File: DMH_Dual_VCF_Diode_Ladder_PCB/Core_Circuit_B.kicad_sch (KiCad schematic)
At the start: 53 parts, among them SW1 SW_SPDT, SW2 SW_SPDT, SW3 SW_SPDT, SW5 Switch_SP3T_APEM5244, U1 TL074, U2 TL074

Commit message: Schematic design in progress
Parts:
- renumbered C11 to C18, C12 to C19, C15 to C20, C13 to C21, C14 to C22, C7 to C3, C10 to C6, D14 to D15, D13 to D16, D7 to D17, D8 to D18, D9 to D19, D10 to D20, D11 to D21, D12 to D22, D6 to D23, R19 to R63, R18 to R64, R14 to R65, R16 to R66, R5 to R67, R17 to R68, R15 to R69, R6 to R70, R21 to R71, R2 to R72, R20 to R73, R23 to R74, R1 to R75, R22 to R76, R3 to R77, R7 to R78, R10 to R79, R13 to R80, R11 to R81, R4 to R82, R9 to R83, R8 to R84, R12 to R85, R61 to R86, R24 to R87, R62 to R88, RV1 to RV16, RV2 to RV17, RV3 to RV18, RV4 to RV19, RV6 to RV5, SW5 to SW10, SW3 to SW7, SW1 to SW8, SW2 to SW9, U1 to U5, U2 to U6

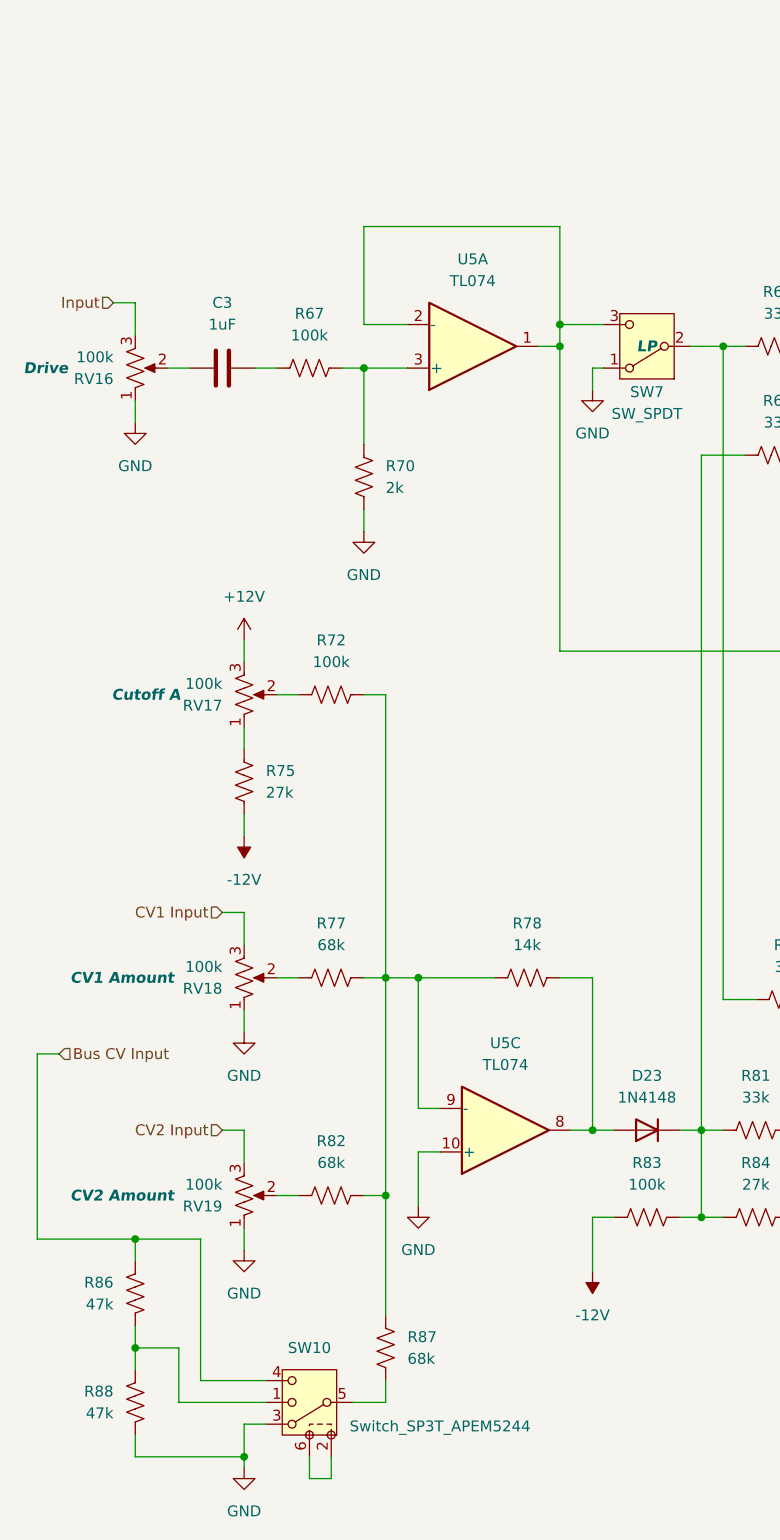
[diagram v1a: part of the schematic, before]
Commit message: Made CV processing page
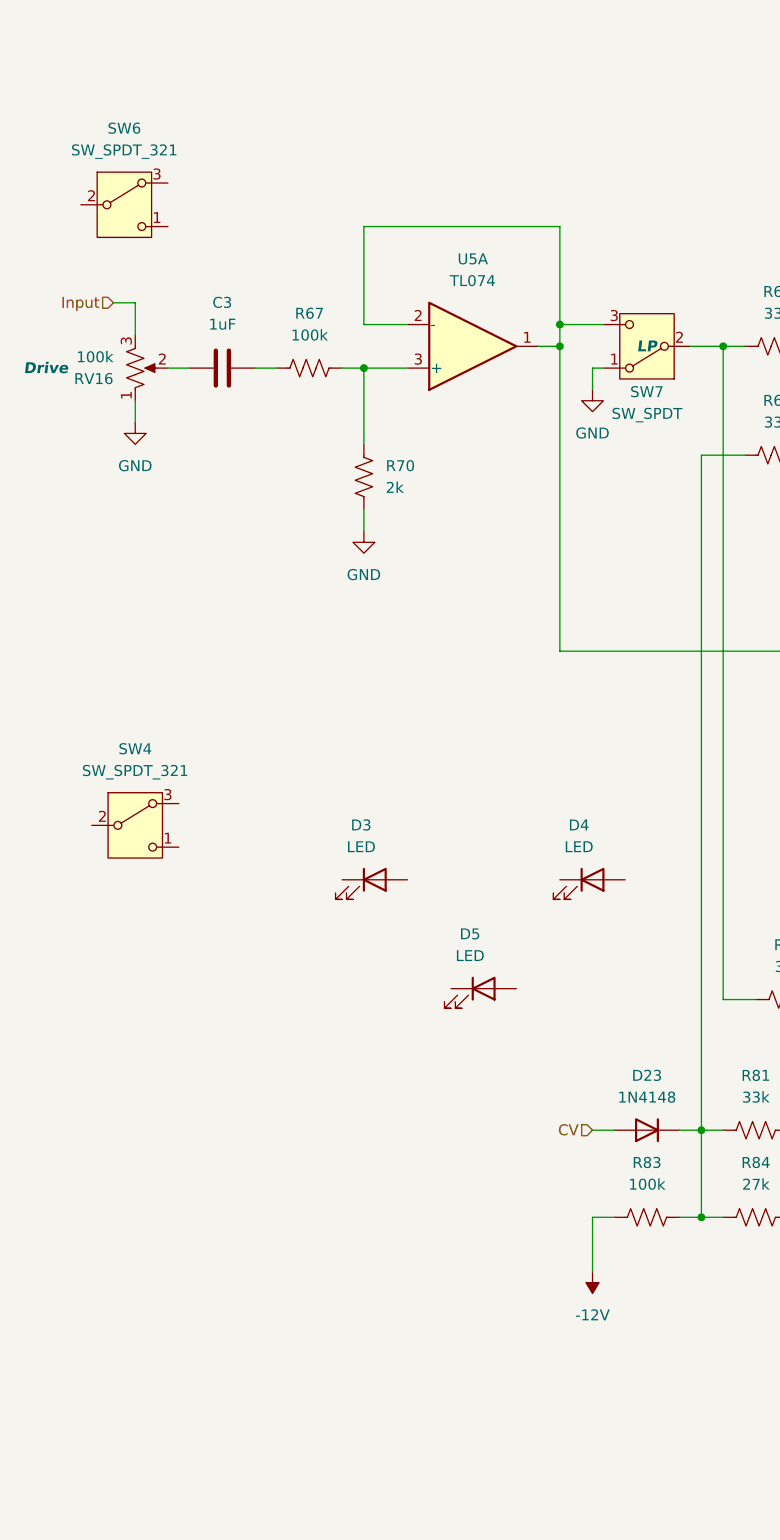
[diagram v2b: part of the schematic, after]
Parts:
- removed R72: 100k, Resistor_THT:R_Axial_DIN0207_L6.3mm_D2.5mm_P7.62mm_Horizontal, symbol Device:R_US
- removed R75: 27k, Resistor_THT:R_Axial_DIN0207_L6.3mm_D2.5mm_P7.62mm_Horizontal, symbol Device:R_US
- removed R77, R82, R87: 68k, Resistor_THT:R_Axial_DIN0207_L6.3mm_D2.5mm_P7.62mm_Horizontal, symbol Device:R_US
- removed R78: 14k, Resistor_THT:R_Axial_DIN0207_L6.3mm_D2.5mm_P7.62mm_Horizontal, symbol Device:R_US
- removed R86, R88: 47k, Resistor_THT:R_Axial_DIN0207_L6.3mm_D2.5mm_P7.62mm_Horizontal, symbol Device:R_US
- removed RV17: 100k, SynthStuff:Potentiometer_Alpha_RD901F-40-00D_Single_Vertical, symbol Device:R_Potentiometer_US
- removed RV18, RV19: 100k, SynthStuff:Potentiometer_TT_P110KH1, symbol Device:R_Potentiometer_US
- removed SW10: Switch_SP3T_APEM5244, symbol SynthStuff:Switch_SP3T
- removed unit 3 of U5
- added D3, D4, D5: LED, LED_THT:LED_D3.0mm, symbol Device:LED
- added SW4, SW6: SW_SPDT_321, SynthStuff:Toggle_Switch_THT, symbol Switch:SW_SPDT_321
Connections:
- net CV: now reaches D23.2 (A)

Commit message: Finished designing circuit
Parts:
- removed D3, D4, D5: LED, LED_THT:LED_D3.0mm, symbol Device:LED
- removed SW4, SW6: SW_SPDT_321, SynthStuff:Toggle_Switch_THT, symbol Switch:SW_SPDT_321

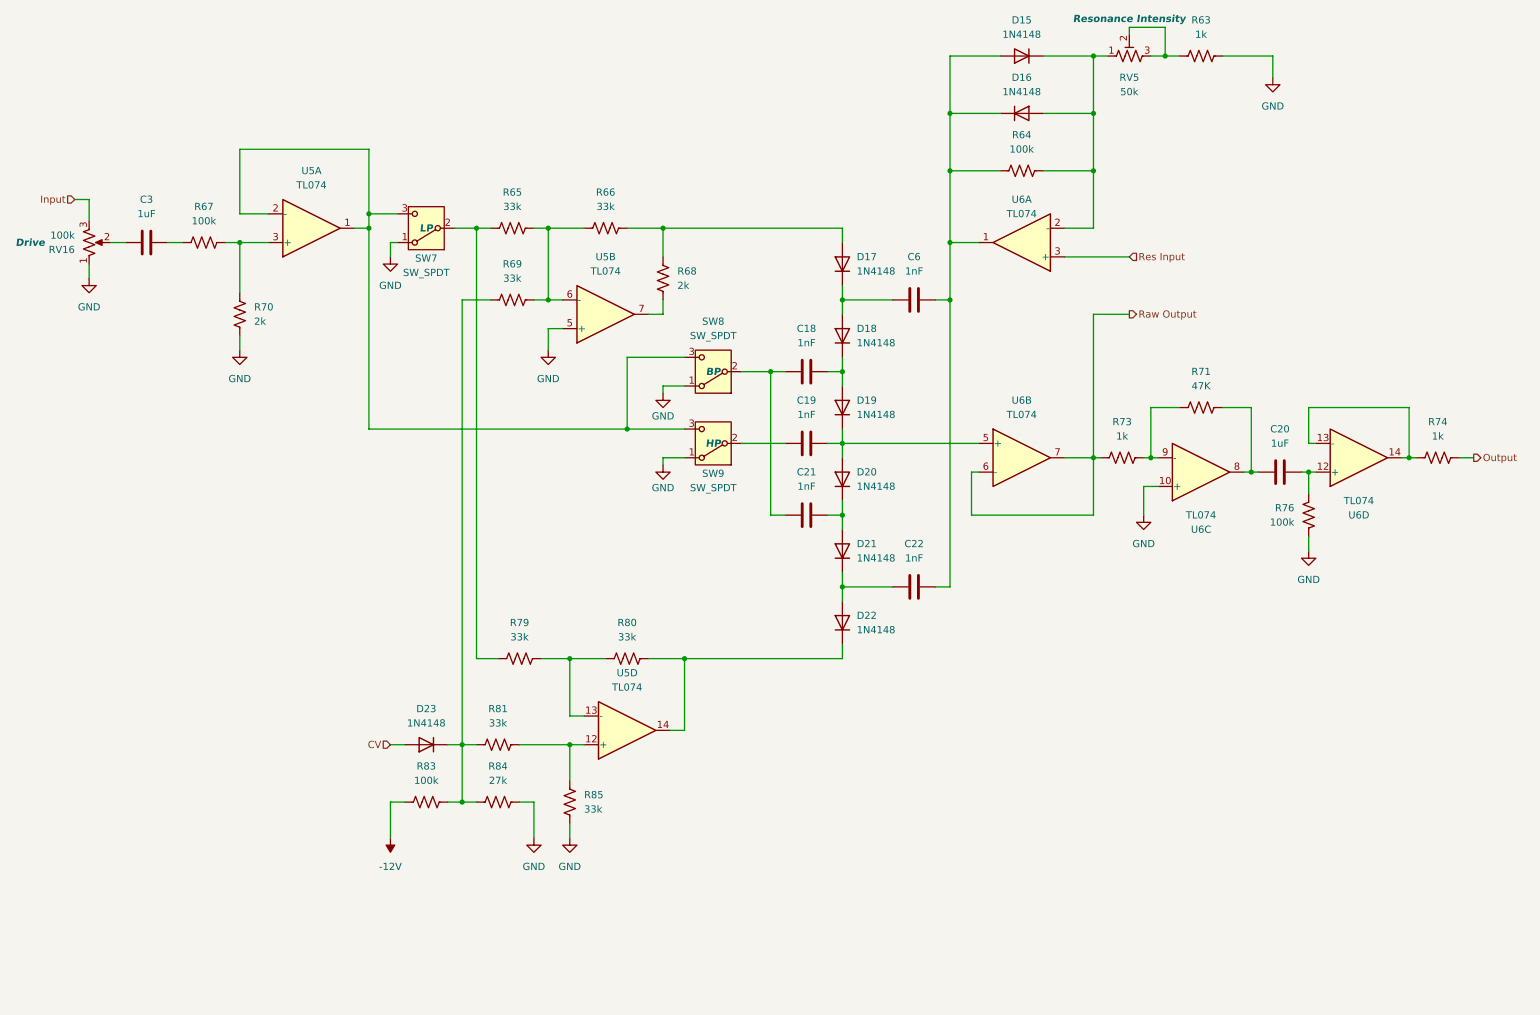
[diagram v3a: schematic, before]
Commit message: Reannotated whole schematic
OpAmp annotation is still tentative.
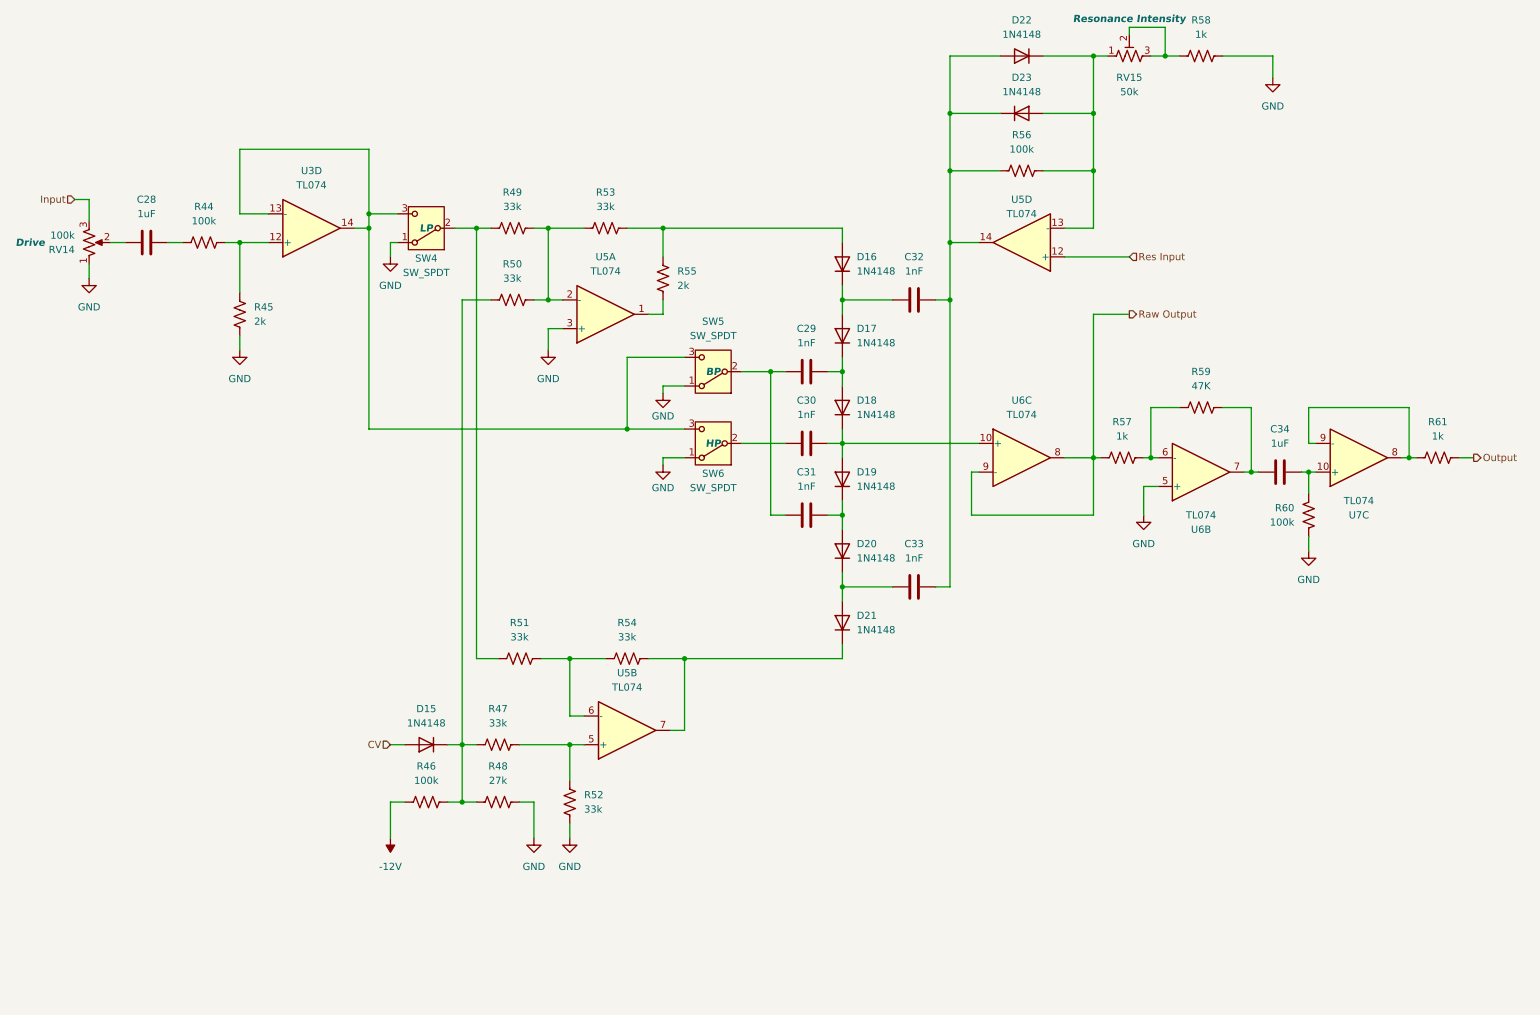
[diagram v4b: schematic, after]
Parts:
- renumbered C3 to C28, C18 to C29, C19 to C30, C21 to C31, C6 to C32, C22 to C33, C20 to C34, D23 to D15, D17 to D16, D18 to D17, D19 to D18, D20 to D19, D21 to D20, D22 to D21, D15 to D22, D16 to D23, R67 to R44, R70 to R45, R83 to R46, R81 to R47, R84 to R48, R65 to R49, R69 to R50, R79 to R51, R85 to R52, R66 to R53, R80 to R54, R68 to R55, R64 to R56, R73 to R57, R63 to R58, R71 to R59, R76 to R60, R74 to R61, RV16 to RV14, RV5 to RV15, SW7 to SW4, SW8 to SW5, SW9 to SW6, U5 to U3, U6 to U5, U6 to U7
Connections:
- net GND: now also U5.3 (+), U6.5 (+); no longer U5.5 (+), U6.10 (+)
- net Raw Output: now also U6.8, U6.9 (-); no longer U6.6 (-), U6.7
- net Res Input: now also U5.12 (+); no longer U5.3 (+)
- net at C30.2, D18.1 (K), D19.2 (A): now also U6.10 (+); no longer U6.5 (+)
- net at R44.2, R45.2: now also U3.12 (+); no longer U3.3 (+)
- net at R55.1: now also U5.1; no longer U5.7
- net at R49.2, R50.2, R53.1: now also U5.2 (-); no longer U5.6 (-)
- net at SW4.3 (C), SW5.3 (C), SW6.3 (C): now also U3.13 (-), U3.14; no longer U3.1, U3.2 (-)
- net at C32.2, C33.2, D22.2 (A)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: now also U5.14; no longer U5.1
- net at D22.1 (K), D23.2 (A), R56.2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: now also U5.13 (-); no longer U5.2 (-)
- net at R51.2, R54.1: now also U5.6 (-); no longer U5.13 (-)
- net at R47.2, R52.2: now also U5.5 (+); no longer U5.12 (+)
- net at C34.2, R60.2: now also U7.10 (+); no longer U7.12 (+)
- net at C34.1, R59.2: now also U6.7; no longer U6.8
- net at R57.2, R59.1: now also U6.6 (-); no longer U6.9 (-)
- net at D21.1 (K), R54.2: now also U5.7; no longer U5.14
- new net: R61.1, U7.8, U7.9 (-)

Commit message: Reannotated OpAmps and cleared errors
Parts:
- renumbered U5 to U4, U6 to U4, U7 to U5, U5 to U6
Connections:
- net GND: now also U6.3 (+); no longer U6.5 (+)
- net at C34.2, R60.2: now also U5.5 (+); no longer U5.10 (+)
- net at R57.2, R59.1: now also U6.2 (-); no longer U6.6 (-)
- net at C34.1, R59.2: now also U6.1; no longer U6.7
- new net: R61.1, U5.6 (-), U5.7
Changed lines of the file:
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@@
 		(on_board yes)
 		(dnp no)
-		(property "Reference" "U5"
+		(property "Reference" "U4"
 			(at 190.5 55.88 0)
 			(effects
@@
 			(project "DMH_Dual_VCF_Diode_Ladder_PCB"
 				(path "/58f4306d-5387-4983-bb08-41a2313fd315/5770dcd3-eb9e-472f-b743-1e3eb22ed082"
-					(reference "U5")
+					(reference "U4")
 					(unit 4)
 				)
@@
 		(at 250.19 101.6 0)
 		(mirror x)
-		(unit 3)
-		(exclude_from_sim no)
-		(in_bom yes)
-		(on_board yes)
-		(dnp no)
-		(property "Reference" "U7"
+		(unit 2)
+		(exclude_from_sim no)
+		(in_bom yes)
+		(on_board yes)
+		(dnp no)
+		(property "Reference" "U5"
 			(at 250.19 111.76 0)
 			(effects
@@
 			(project "DMH_Dual_VCF_Diode_Ladder_PCB"
 				(path "/58f4306d-5387-4983-bb08-41a2313fd315/5770dcd3-eb9e-472f-b743-1e3eb22ed082"
-					(reference "U7")
-					(unit 3)
+					(reference "U5")
+					(unit 2)
 				)
 			)
@@
 		(at 222.25 104.14 0)
 		(mirror x)
-		(unit 2)
+		(unit 1)
 		(exclude_from_sim no)
 		(in_bom yes)
@@
 				(path "/58f4306d-5387-4983-bb08-41a2313fd315/5770dcd3-eb9e-472f-b743-1e3eb22ed082"
 					(reference "U6")
-					(unit 2)
+					(unit 1)
 				)
 			)
@@
 		(dnp no)
 		(fields_autoplaced yes)
-		(property "Reference" "U6"
+		(property "Reference" "U4"
 			(at 190.5 91.44 0)
 			(effects
@@
 			(project "DMH_Dual_VCF_Diode_Ladder_PCB"
 				(path "/58f4306d-5387-4983-bb08-41a2313fd315/5770dcd3-eb9e-472f-b743-1e3eb22ed082"
-					(reference "U6")
+					(reference "U4")
 					(unit 3)
 				)
@@
 		(dnp no)
 		(fields_autoplaced yes)
-		(property "Reference" "U5"
+		(property "Reference" "U6"
 			(at 120.65 139.7 0)
 			(effects
@@
 			(project "DMH_Dual_VCF_Diode_Ladder_PCB"
 				(path "/58f4306d-5387-4983-bb08-41a2313fd315/5770dcd3-eb9e-472f-b743-1e3eb22ed082"
-					(reference "U5")
+					(reference "U6")
 					(unit 2)
 				)

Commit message: Updated switches symbols and fps
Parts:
- SW4, SW5, SW6: footprint SynthStuff:Toggle_Switch_THT -> SynthStuff:Toggle_Switch_TE
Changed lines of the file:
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@@
 			)
 		)
-		(property "Footprint" "SynthStuff:Toggle_Switch_THT"
+		(property "Footprint" "SynthStuff:Toggle_Switch_TE"
 			(at 135.89 86.36 0)
 			(effects
@@
 			)
 		)
-		(property "Footprint" "SynthStuff:Toggle_Switch_THT"
+		(property "Footprint" "SynthStuff:Toggle_Switch_TE"
 			(at 135.89 99.06 0)
 			(effects
@@
 			)
 		)
-		(property "Footprint" "SynthStuff:Toggle_Switch_THT"
+		(property "Footprint" "SynthStuff:Toggle_Switch_TE"
 			(at 85.09 60.96 0)
 			(effects
